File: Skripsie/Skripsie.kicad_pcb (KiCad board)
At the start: 2 copper layers, 200 x 165 mm, 291 parts, among them J1 STM32F4_Discovery, J10 LED_R_TEST, J11 3V3, J12 UART_TEST, J13 USB_B, J2 LCD_TEST, J3 BTN_C_TEST, J4 LED_C_TEST, J5 LED_SER_TEST, J6 BTN_SER_TEST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

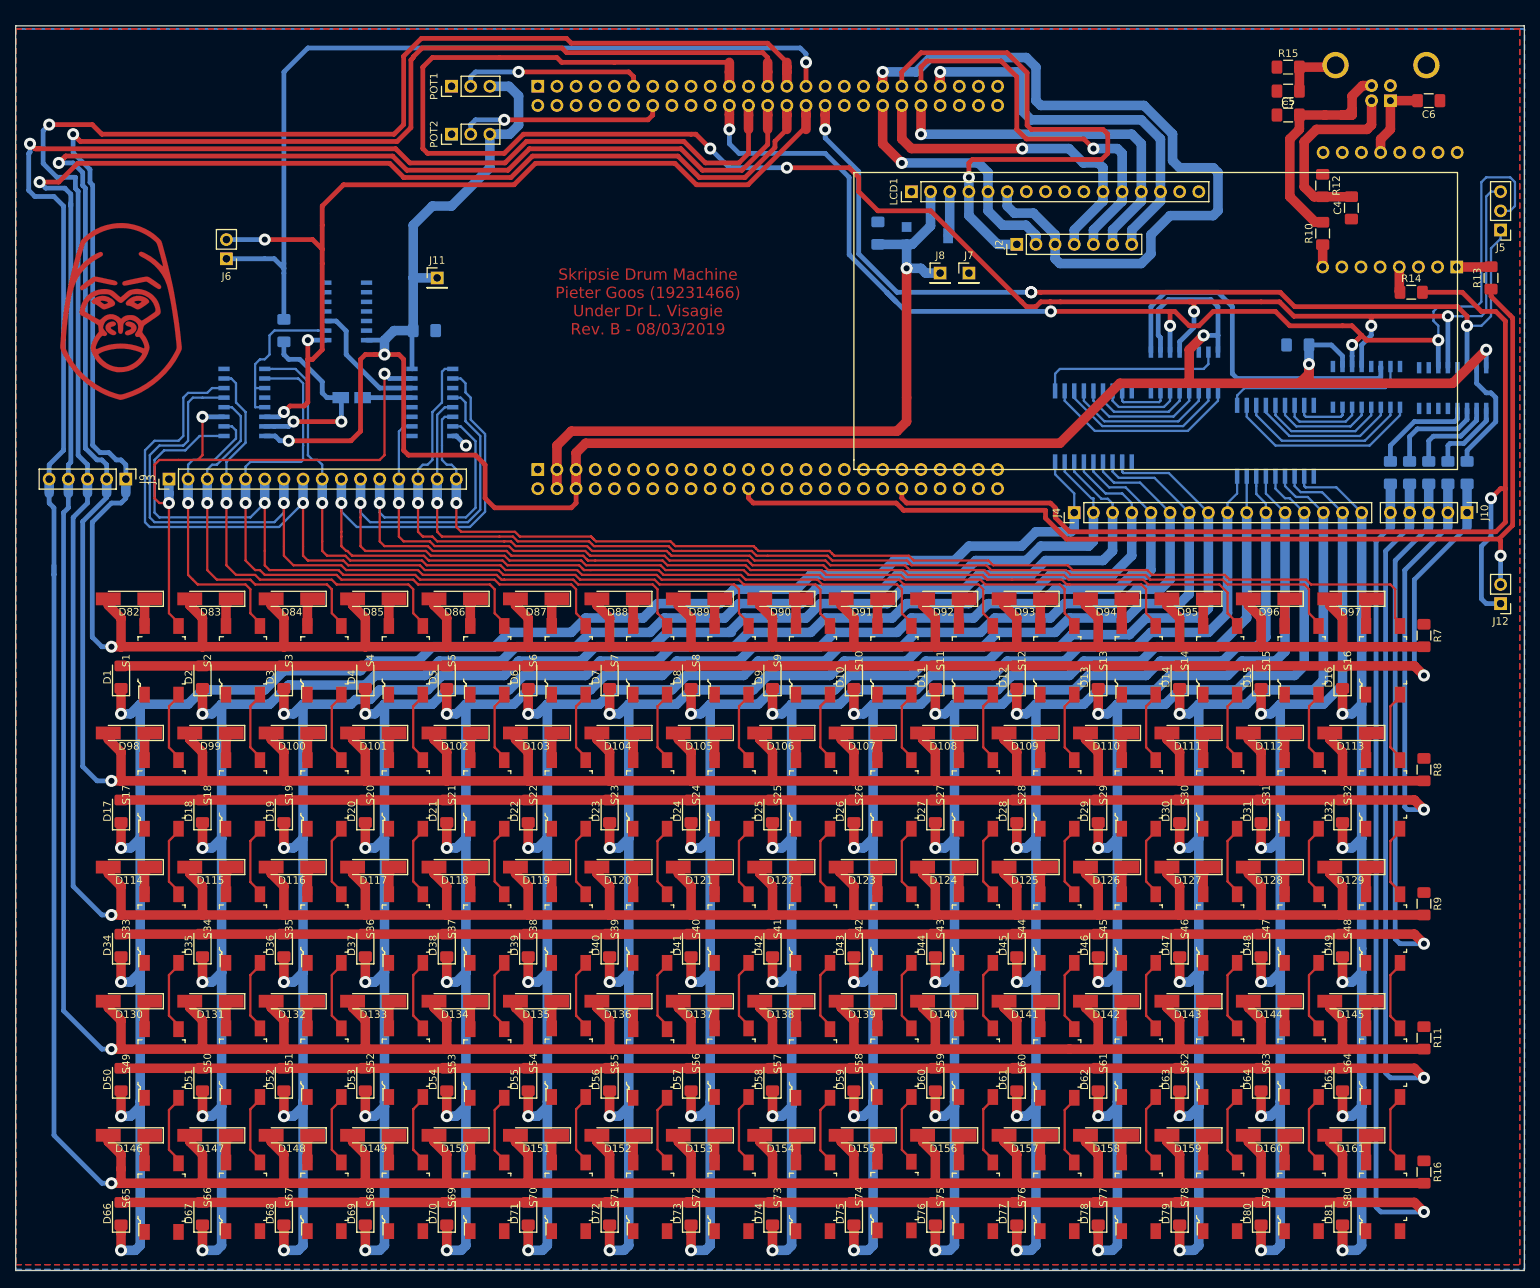
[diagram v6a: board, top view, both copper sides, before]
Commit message: Corrected PCB Missing Traces & Updated to Rev C
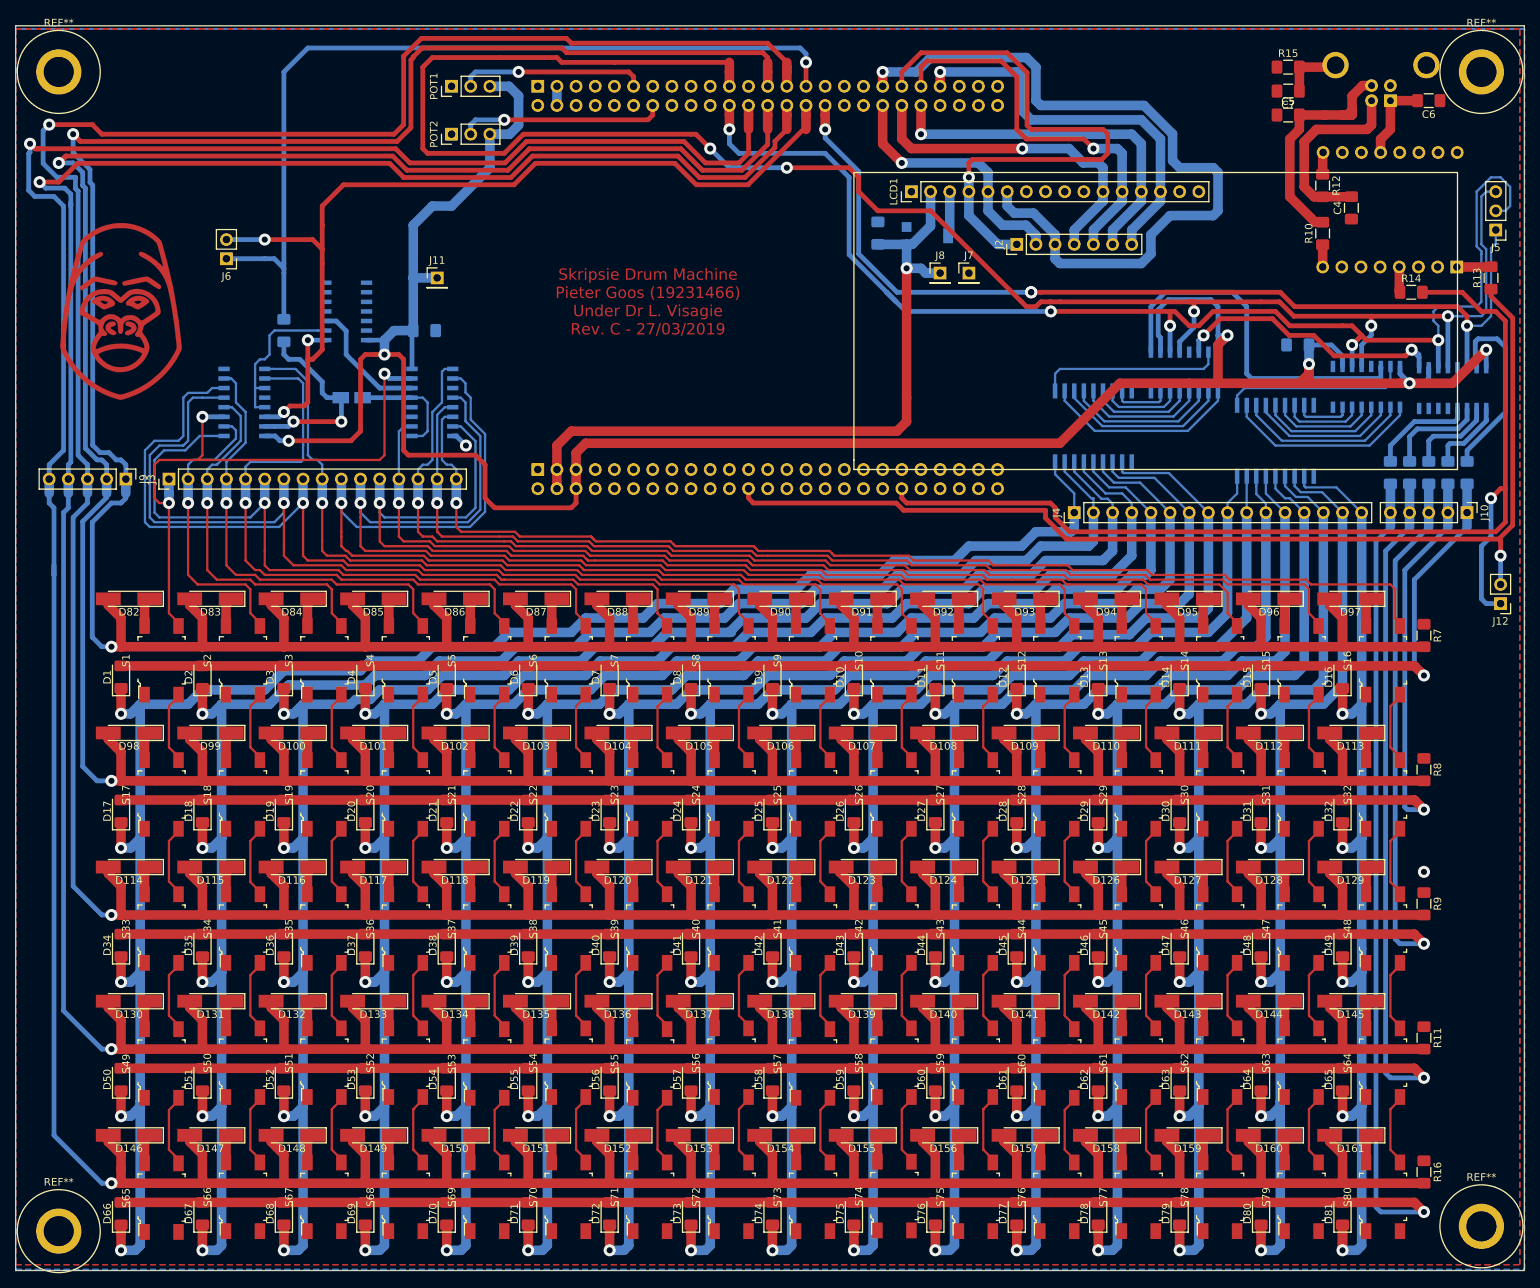
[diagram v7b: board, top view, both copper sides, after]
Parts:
- added REF**: Banana_Jack_1Pin, Connector:Banana_Jack_1Pin, F.Cu at (23.5, 184.8)
- added REF**: Banana_Jack_1Pin, Connector:Banana_Jack_1Pin, F.Cu at (212.1, 184.2)
- added REF**: Banana_Jack_1Pin, Connector:Banana_Jack_1Pin, F.Cu at (212.1, 31.1)
- added REF**: Banana_Jack_1Pin, Connector:Banana_Jack_1Pin, F.Cu at (23.5, 31.1)
- moved J5 0.63 mm to (214.0, 52.1)
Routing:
- net Net-(U1-Pad9): track 0.00 -> 38.2 mm, vias 0 -> 2
- net Net-(R1-Pad2): track 15.4 -> 25.4 mm
- net Net-(D33-Pad1): track 6.94 -> 15.4 mm
- net +3V3: track 312.9 -> 320.7 mm, vias 5 -> 6
- net Net-(R12-Pad1): track 0.00 -> 2.92 mm
- net USB_5V: track 0.00 -> 2.54 mm
- net LED_RCLK: track 249.0 -> 250.6 mm
- net BTN_R4: track 540.4 -> 541.3 mm
- net LED_SRCLK: track 171.2 -> 170.3 mm
- net GND: vias 1 -> 2
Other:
- board text added: "Skripsie Drum Machine Pieter Goos (19231466) Under Dr L. Visagie Rev. C - 27/03/2019"
- board text removed: "Skripsie Drum Machine Pieter Goos (19231466) Under Dr L. Visagie Rev. B - 08/03/2019"

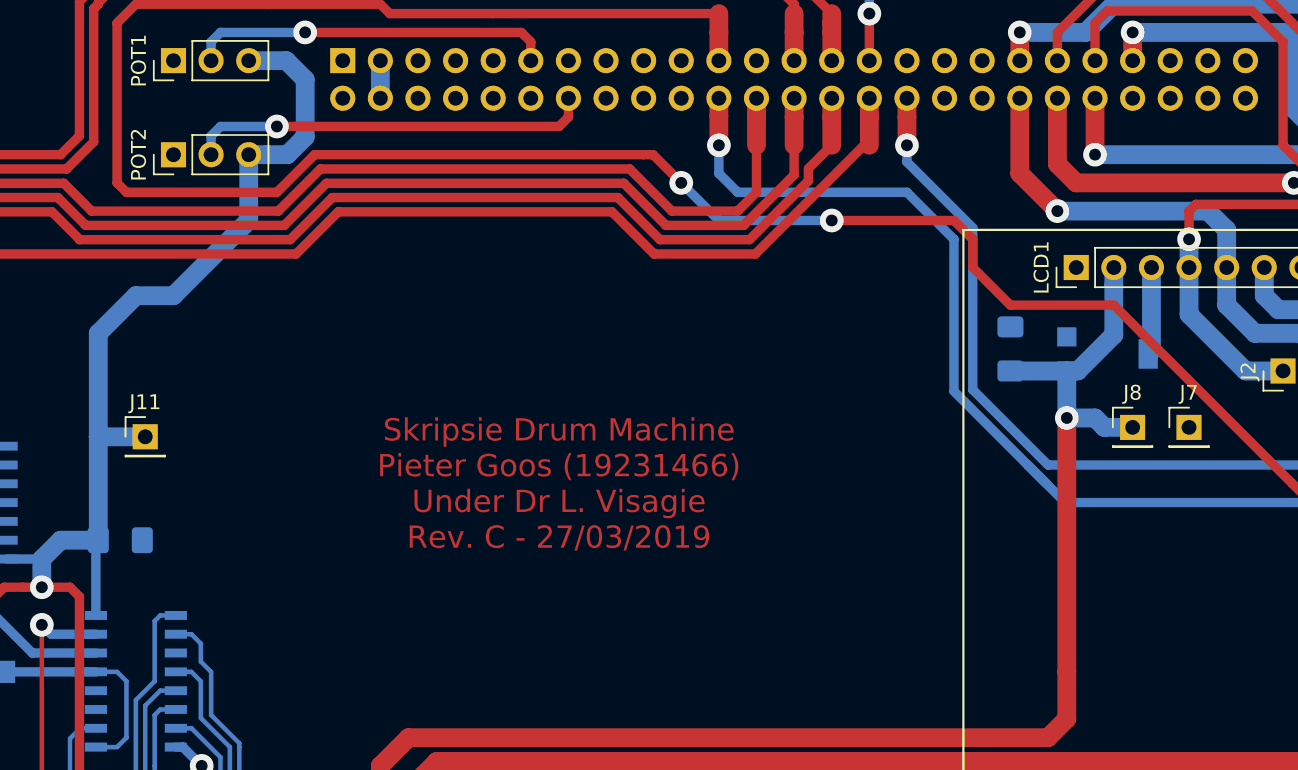
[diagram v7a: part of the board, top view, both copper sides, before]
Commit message: Button Row 4 changed from PB2 to PC4 due to onboard resistors
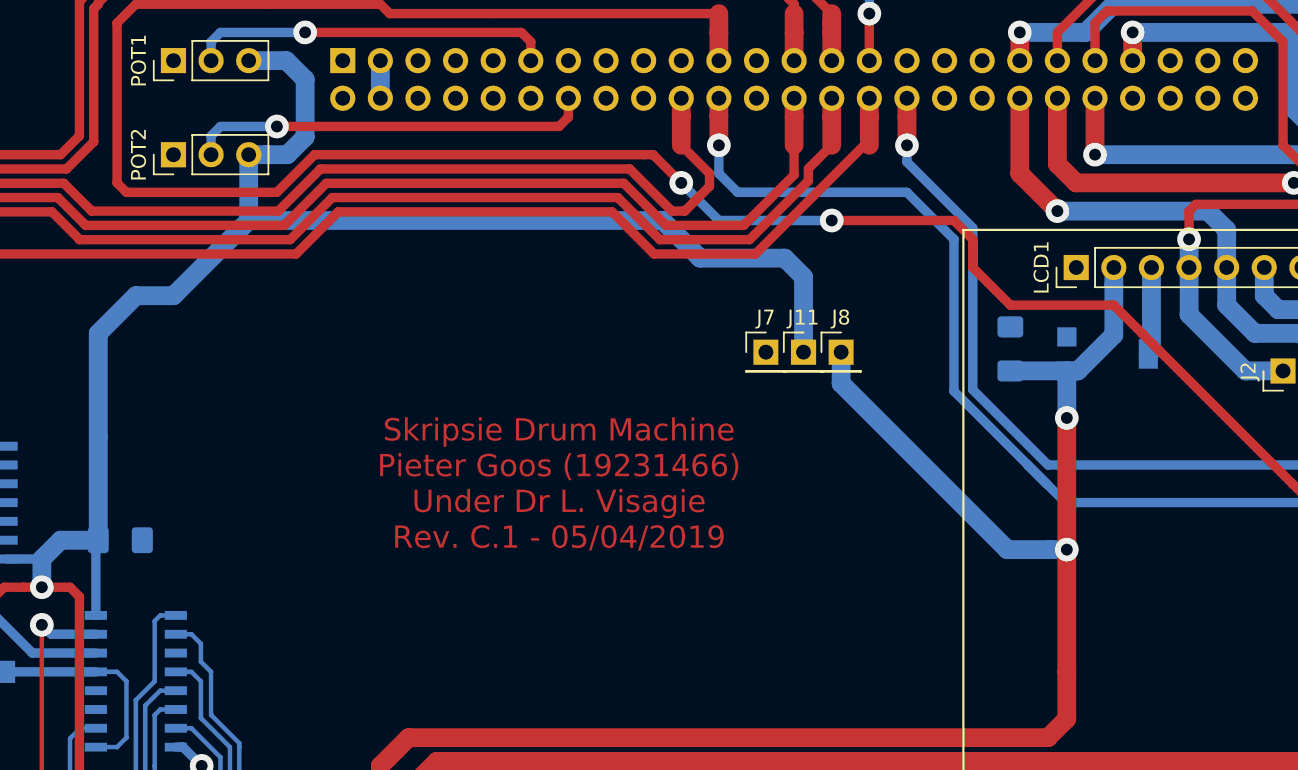
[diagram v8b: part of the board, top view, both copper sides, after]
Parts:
- moved J11 44.8 mm to (118.1, 52.7)
- moved J7 29.0 mm to (115.6, 52.7)
- moved J8 20.3 mm to (120.7, 52.7)
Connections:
- J1 pad 39: BTN_R4 -> Net-(J1-Pad39)
- J1 pad 41: Net-(J1-Pad41) -> BTN_R4
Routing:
- net +3V3: track 320.7 -> 361.6 mm
- net +5V: track 94.1 -> 111.4 mm, vias 1 -> 2
- net BTN_R4: track 541.3 -> 538.7 mm
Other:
- board text added: "Skripsie Drum Machine Pieter Goos (19231466) Under Dr L. Visagie Rev. C.1 - 05/04/2019"
- board text removed: "Skripsie Drum Machine Pieter Goos (19231466) Under Dr L. Visagie Rev. C - 27/03/2019"
